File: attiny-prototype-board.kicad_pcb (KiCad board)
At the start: 2 copper layers, 160 x 100 mm, 51 parts, among them J1 Banana, J10 banana, J11 banana, J12 banana, J13 tinyLeft, J14 TRS35, J15 toPoti, J16 toAudio, J17 USART, J18 TRS35, J19 toPoti, J2 Banana, J20 GND, J21 toBtn, J22 toPoti, J23 VCC, J25 I2C, J3 Banana, J4 Banana, J5 tinyRight, J6 toPoti, J7 tinyRight, J8 tinyRight, J9 banana, SW1 SW_SPDT, SW2 Switch UPDI, SW3 SW_Push, SW4 SW_SPDT, SW5 SW_Push, SW6 SW_SPDT, SW7 SW_SPDT, U1 FTDI-Adapter, U2 ATtinyXX14-SS

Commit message: v2.1 some improvements
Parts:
- removed SW5: SW_Push, ftdi:PushBtn6x6
- removed SW6, SW7: SW_SPDT, ftdi:Switch_SPDT_1P2T
- added SW10: SW_Push_DPDT, ftdi:PushBtn6x6, F.Cu at (161.5, 115.7)
- added SW8: 2x Switch, ftdi:Switch_SPDT_2P2T, F.Cu at (57.1, 100.5)
- added SW9: SW_Push_DPDT, ftdi:PushBtn6x6, F.Cu at (170.7, 115.6)
- R5, R6: value 10k -> 1.5k
- SW3: value SW_Push -> 2x Switch; footprint ftdi:PushBtn6x6 -> ftdi:Switch_SPDT_2P2T
- U1: footprint ftdi:FTDI -> AudioChannel:FTDI
- moved SW3 31.4 mm to (190.8, 104.0), turned to 180 degrees
- moved R6 19.2 mm to (46.2, 101.5), turned to 0 degrees
- moved R5 14.5 mm to (47.9, 107.0), turned to 180 degrees
- moved J25 14.0 mm to (70.6, 105.5), turned to 270 degrees
- moved J5 5.53 mm to (182.1, 83.8)
- moved J8 5.53 mm to (184.6, 93.8)
- moved SW1 5.53 mm to (191.8, 79.8)
- moved SW4 5.53 mm to (191.8, 69.2)
- moved J1 1.27 mm to (77.8, 26.3)
- moved J10 1.27 mm to (119.7, 37.2)
- moved J11 1.27 mm to (179.8, 37.2)
- moved J12 1.27 mm to (149.8, 37.2)
- moved J2 1.27 mm to (167.4, 26.5)
- moved J3 1.27 mm to (107.2, 26.3)
- moved J4 1.27 mm to (137.2, 26.5)
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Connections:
- J21 pad 2: Net-(J21-Pad1) -> Net-(J21-Pad2)
- J21 pad 4: Net-(J21-Pad3) -> Net-(J21-Pad1)
- J21 pad 6: Net-(J21-Pad5) -> Net-(J21-Pad6)
- J21 pad 8: Net-(J21-Pad7) -> Net-(J21-Pad5)
- J25 pad 7: Net-(J25-Pad7) -> SDA
- J25 pad 8: Net-(J25-Pad8) -> SCL
- R5 pad 1: Net-(J25-Pad7) -> Net-(R5-Pad1)
- R6 pad 2: Net-(J25-Pad8) -> Net-(R6-Pad2)
- SW3 pad 1: Net-(J21-Pad1) -> Net-(J8-Pad10)
- SW3 pad 2: Net-(J21-Pad3) -> Net-(J8-Pad11)
- SW3 pad 3: (no net) -> Net-(J8-Pad7)
- SW3 pad 4: (no net) -> Net-(J8-Pad3)
- SW3 pad 5: (no net) -> Net-(J8-Pad5)
- SW3 pad 6: (no net) -> Net-(J8-Pad1)
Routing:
- net Net-(J21-Pad3): track 11.1 -> 24.0 mm
- net VCC: track 151.8 -> 141.6 mm
- net Net-(J21-Pad2): track 0.00 -> 8.96 mm
- net Net-(R5-Pad1): track 0.00 -> 7.37 mm
- net Net-(R6-Pad2): track 0.00 -> 7.12 mm
- net Net-(J21-Pad6): track 0.00 -> 6.46 mm
- net Net-(J8-Pad7): track 13.0 -> 8.85 mm
- net Net-(J25-Pad7): track 3.71 -> 0.00 mm
- net Net-(J25-Pad8): track 3.50 -> 0.00 mm
- net Net-(J8-Pad11): track 13.0 -> 15.8 mm
- net Net-(J8-Pad10): track 13.0 -> 15.8 mm
- net Net-(J8-Pad3): track 13.3 -> 15.7 mm
- net SDA: track 58.4 -> 56.5 mm
- net SCL: track 51.5 -> 52.4 mm
- net Net-(J21-Pad5): track 11.0 -> 10.1 mm
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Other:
- board text added: "PullUp"
- board text added: "Push to ..."
- board text added: "SB v2.1 ma-ha (c) 2023"
- board text added: "close"
- board text added: "open"
- board text removed: "10k PullUp"
- board text removed: "SB v2.0 ma-ha (c) 2023"

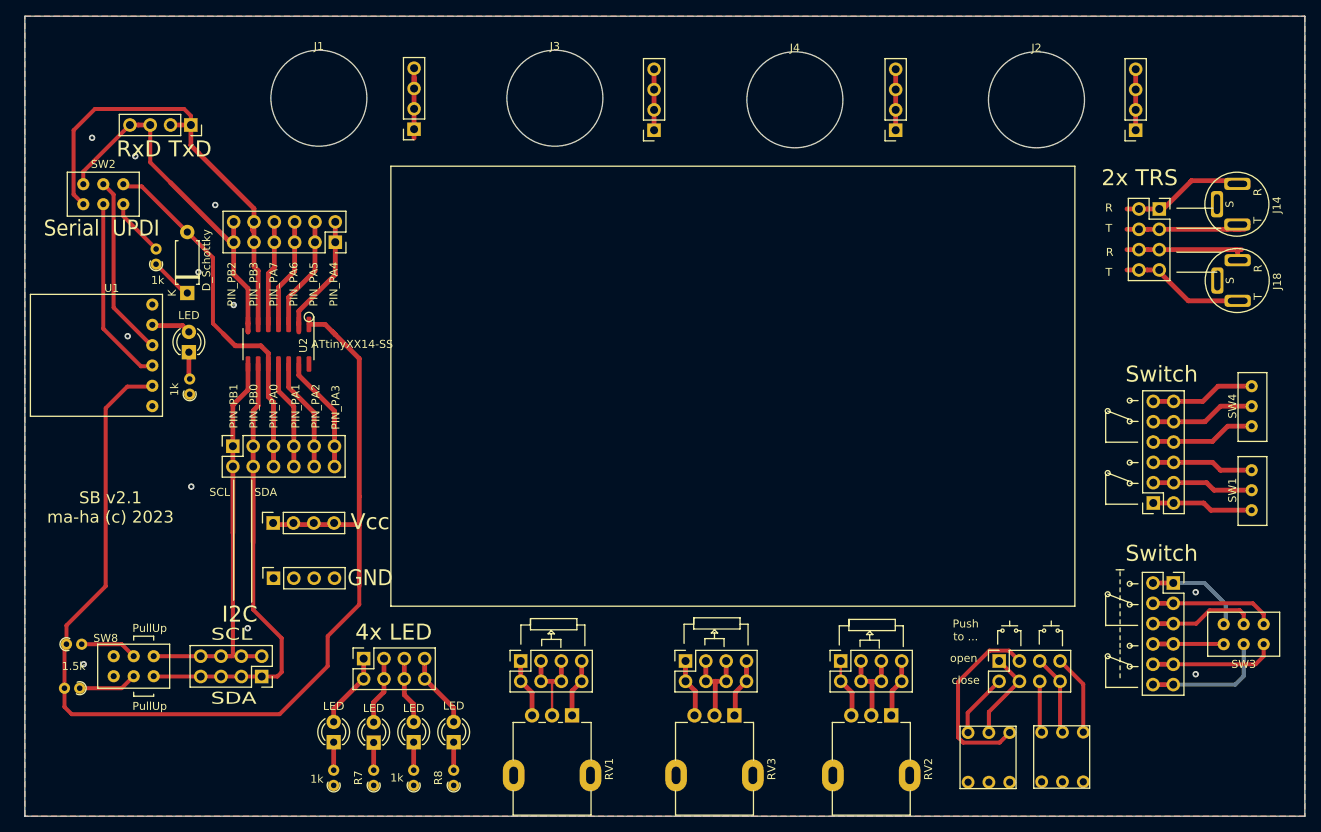
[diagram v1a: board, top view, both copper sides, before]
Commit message: v2.1 move USART
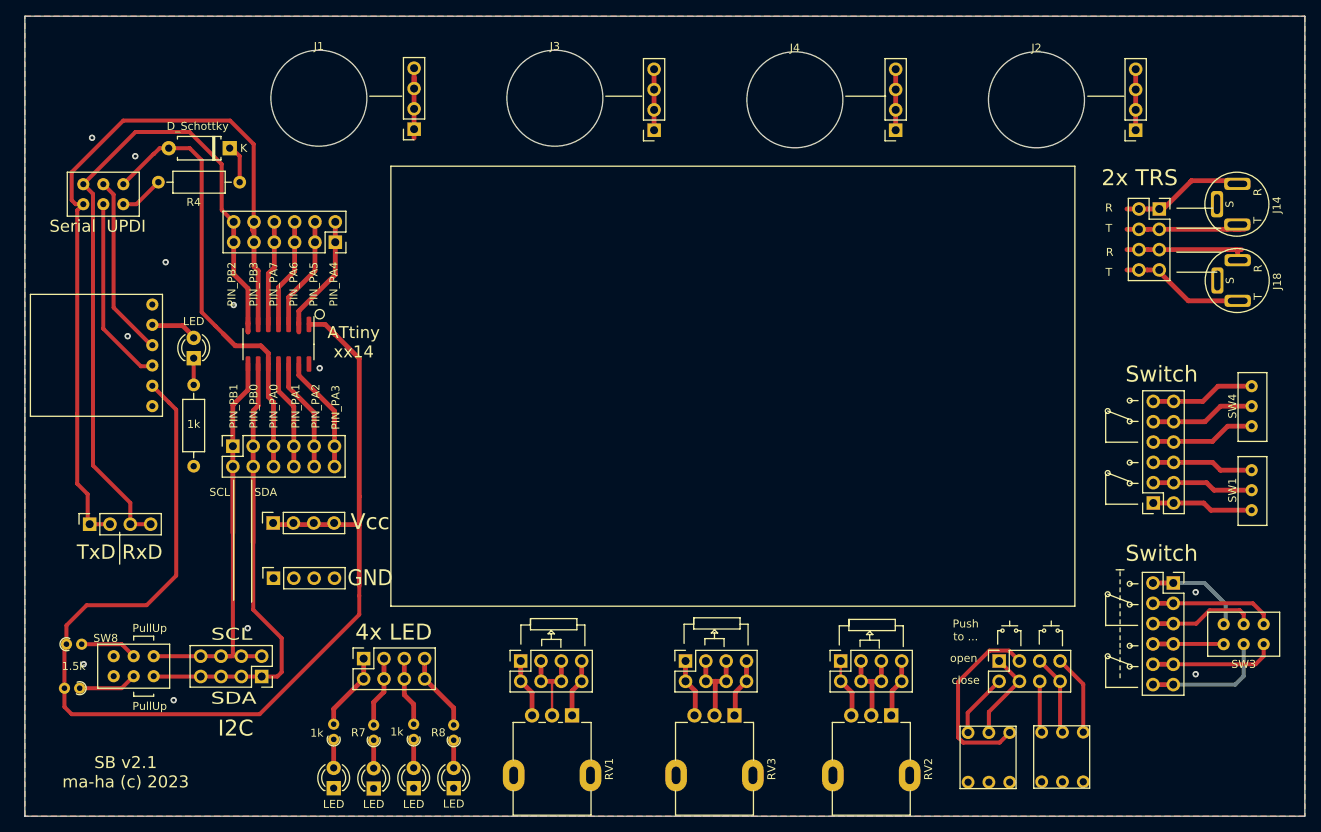
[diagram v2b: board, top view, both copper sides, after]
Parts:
- removed R3: 1k, Resistor_THT:R_Axial_DIN0204_L3.6mm_D1.6mm_P1.90mm_Vertical
- added 1k: 1k, Resistor_THT:R_Axial_DIN0207_L6.3mm_D2.5mm_P10.16mm_Horizontal, F.Cu at (62.1, 79.2)
- R4: footprint Resistor_THT:R_Axial_DIN0204_L3.6mm_D1.6mm_P1.90mm_Vertical -> Resistor_THT:R_Axial_DIN0207_L6.3mm_D2.5mm_P10.16mm_Horizontal
- moved J17 51.5 mm to (49.1, 86.5), turned to 90 degrees
- moved D4 18.9 mm to (66.6, 39.5), turned to 180 degrees
- moved R4 14.6 mm to (67.8, 43.8), turned to 180 degrees
- moved D1 5.75 mm to (79.6, 119.5)
- moved D2 5.75 mm to (84.6, 119.5)
- moved D5 5.75 mm to (89.6, 119.5)
- moved D6 5.75 mm to (94.6, 119.5)
- moved R1 5.75 mm to (79.6, 113.4)
- moved R2 5.75 mm to (89.6, 113.4)
- moved R7 5.65 mm to (84.6, 113.5)
- moved R8 5.65 mm to (94.6, 113.5)
- moved D3 0.96 mm to (62.1, 65.8)
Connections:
- D1 pad 1: Net-(D1-Pad1) -> GND
- D2 pad 1: Net-(D2-Pad1) -> GND
- D5 pad 1: Net-(D5-Pad1) -> GND
- D6 pad 1: Net-(D6-Pad1) -> GND
- J6 pad 1: Net-(D1-Pad2) -> Net-(J6-Pad1)
- J6 pad 2: Net-(D1-Pad2) -> Net-(J6-Pad1)
- J6 pad 3: Net-(D2-Pad2) -> Net-(J6-Pad3)
- J6 pad 4: Net-(D2-Pad2) -> Net-(J6-Pad3)
- J6 pad 5: Net-(D5-Pad2) -> Net-(J6-Pad5)
- J6 pad 6: Net-(D5-Pad2) -> Net-(J6-Pad5)
- J6 pad 7: Net-(D6-Pad2) -> Net-(J6-Pad7)
- J6 pad 8: Net-(D6-Pad2) -> Net-(J6-Pad7)
- R1 pad 1: GND -> Net-(D1-Pad2)
- R1 pad 2: Net-(D1-Pad1) -> Net-(J6-Pad1)
- R2 pad 1: GND -> Net-(D5-Pad2)
- R2 pad 2: Net-(D5-Pad1) -> Net-(J6-Pad5)
- R7 pad 1: GND -> Net-(D2-Pad2)
- R7 pad 2: Net-(D2-Pad1) -> Net-(J6-Pad3)
- R8 pad 1: GND -> Net-(D6-Pad2)
- R8 pad 2: Net-(D6-Pad1) -> Net-(J6-Pad7)
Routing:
- net RXD: track 47.6 -> 92.9 mm
- net TXD: track 59.6 -> 98.9 mm
- net TinyP9: track 46.1 -> 56.2 mm
- net Net-(J6-Pad1): track 0.00 -> 9.46 mm
- net Net-(J6-Pad7): track 0.00 -> 9.41 mm
- net Net-(J6-Pad3): track 0.00 -> 8.48 mm
- net Net-(J6-Pad5): track 0.00 -> 8.39 mm
- net Net-(D1-Pad2): track 9.46 -> 3.50 mm
- net Net-(D6-Pad2): track 9.41 -> 3.50 mm
- net Net-(D2-Pad2): track 8.48 -> 3.46 mm
- net Net-(D5-Pad2): track 8.39 -> 3.50 mm
- net VCC: track 141.6 -> 145.4 mm
- net Net-(D6-Pad1): track 3.50 -> 0.00 mm
- net Net-(D5-Pad1): track 3.50 -> 0.00 mm
- net Net-(D1-Pad1): track 3.50 -> 0.00 mm
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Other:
- board text added: "ATtiny xx14"
- board text added: "TxD RxD"
- board text removed: "RxD TxD"
